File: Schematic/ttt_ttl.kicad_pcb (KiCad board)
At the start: 2 copper layers, 79.8 x 129.5 mm, 79 parts, among them J1 Conn_01x01, J2 Conn_01x01, SW1 SW_Push, SW10 SW_Push, SW2 SW_Push, SW3 SW_Push, SW4 SW_Push, SW5 SW_Push, SW6 SW_Push, SW7 SW_Push, SW8 SW_Push, SW9 SW_Push, U1 74LS109, U10 27C2001, U11 74LS154, U12 NE555, U2 74LS109, U3 74LS109, U4 74LS109, U5 74LS109, U6 74LS109, U7 74LS109, U8 74LS109, U9 74LS109

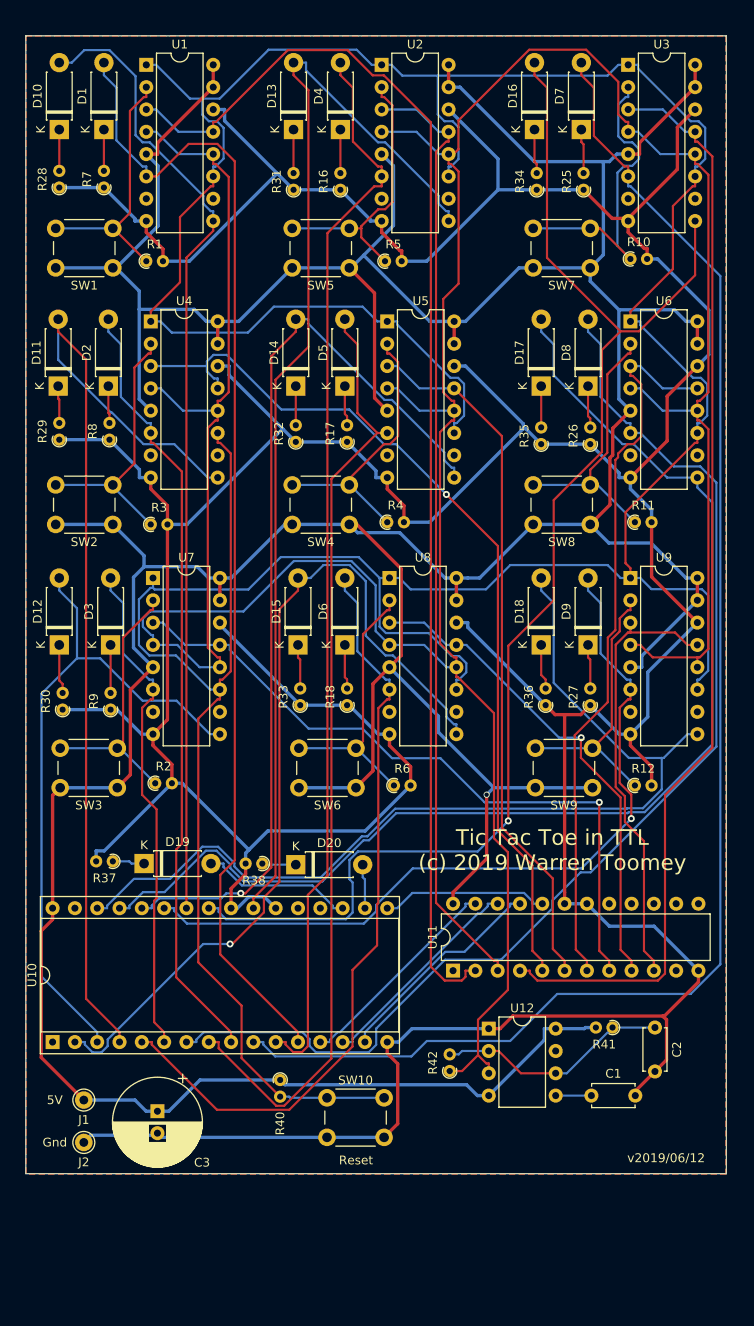
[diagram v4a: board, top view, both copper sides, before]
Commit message: Smaller 8Kx8 EEPROM is working
I managed to get the code to generate a ROM file which uses a 4-bit board
state plus the user's moves to look up the net board move and the next
board state. I've redone the schematic, PCB and I've started on the
documentation. I need to redraw the design diagram.
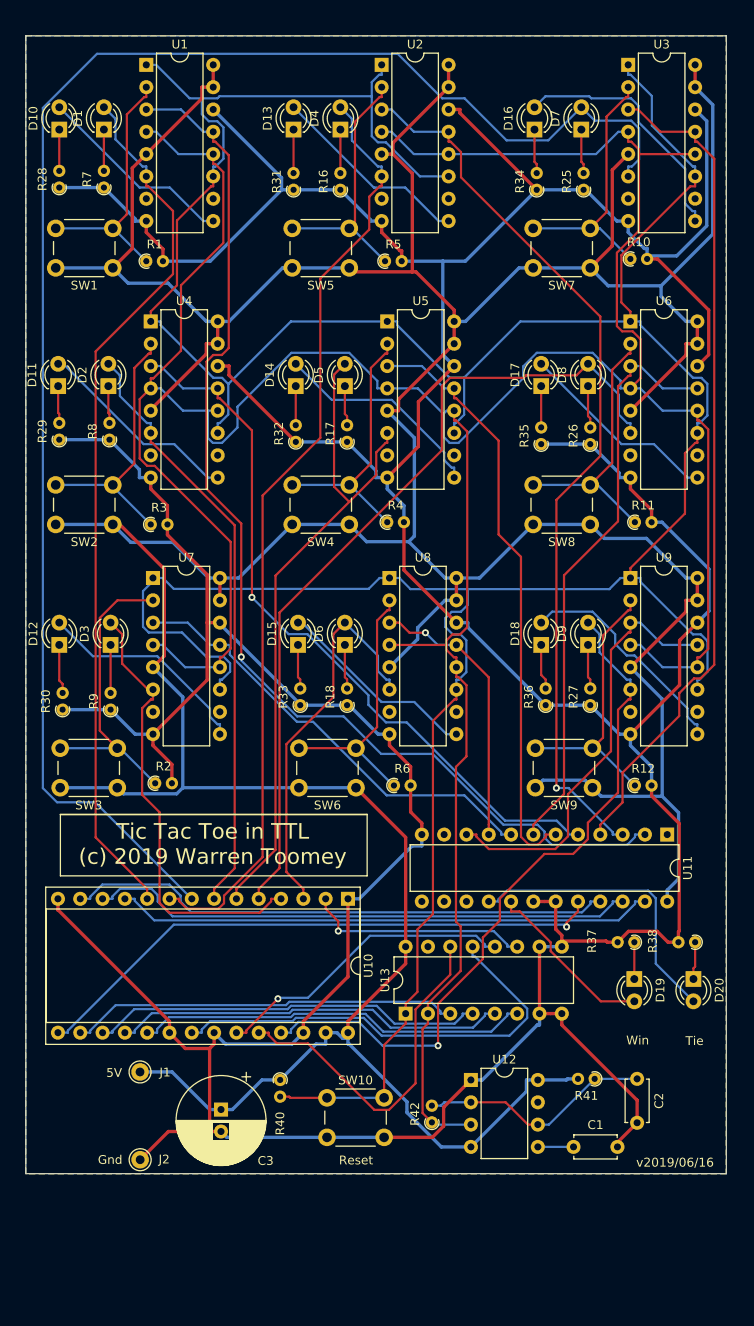
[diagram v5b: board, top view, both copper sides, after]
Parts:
- added U13: 74LS161, Package_DIP:DIP-16_W7.62mm, F.Cu at (67.4, 134.9)
- D1, D10, D11, D12, D13, D14, D15, D16, D17, D18, D19, D2, D20, D3, D4, D5, D6, D7, D8, D9: footprint Diode_THT:D_DO-41_SOD81_P7.62mm_Horizontal -> LED_THT:LED_D3.0mm
- U10: value 27C2001 -> 28C256; footprint Package_DIP:DIP-32_W15.24mm_Socket -> Package_DIP:DIP-28_W15.24mm_Socket
- moved R37 60.1 mm to (93.4, 126.8)
- moved D19 57.3 mm to (93.4, 131.0), turned to 270 degrees
- moved R38 50.1 mm to (100.3, 126.8)
- moved D20 47.1 mm to (100.1, 131.0), turned to 270 degrees
- moved U10 37.4 mm to (60.8, 121.9), turned to 270 degrees
- moved U11 28.9 mm to (97.2, 114.6), turned to 270 degrees
- moved C3 7.24 mm to (46.4, 145.9)
- moved J1 7.16 mm to (37.1, 141.6)
- moved J2 6.71 mm to (37.1, 151.6)
- moved C1 6.19 mm to (86.5, 150.1)
- moved U12 6.19 mm to (74.8, 142.5)
- moved R41 6.19 mm to (88.9, 142.4)
- moved C2 6.19 mm to (93.7, 142.4)
- moved R42 6.19 mm to (70.4, 147.3)
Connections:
- D10 pad 2: Board1 -> Net-(D10-Pad2)
- D11 pad 2: Board4 -> Net-(D11-Pad2)
- D12 pad 2: Board7 -> Net-(D12-Pad2)
- D13 pad 2: Board2 -> Net-(D13-Pad2)
- D14 pad 2: Board5 -> Net-(D14-Pad2)
- D15 pad 2: Board8 -> Net-(D15-Pad2)
- D16 pad 2: Board3 -> Net-(D16-Pad2)
- D17 pad 2: Board6 -> Net-(D17-Pad2)
- D18 pad 2: Board9 -> Net-(D18-Pad2)
- U1 pad 9: Board1 -> Net-(D10-Pad2)
- U10 pad 1: Net-(U10-Pad1) -> Lo
- U10 pad 10: User3 -> User1
- U10 pad 11: User2 -> Net-(U10-Pad11)
- U10 pad 12: User1 -> Net-(U10-Pad12)
- U10 pad 14: Net-(U10-Pad14) -> Lo
- U10 pad 16: Lo -> Net-(U10-Pad16)
- U10 pad 18: Net-(D20-Pad2) -> Net-(U10-Pad18)
- U10 pad 19: Net-(D19-Pad2) -> Net-(U10-Pad19)
- U10 pad 2: Board8 -> Newstate3
- U10 pad 20: Net-(U10-Pad20) -> Lo
- U10 pad 21: Net-(U10-Pad21) -> Newstate1
- U10 pad 23: Board2 -> Newstate2
- U10 pad 24: Lo -> Newstate0
- U10 pad 25: Board3 -> User9
- U10 pad 26: Board1 -> Lo
- U10 pad 27: User9 -> Hi
- U10 pad 28: Board5 -> Hi
- U10 pad 3: Board7 -> User8
- U10 pad 4: Board4 -> User7
- U10 pad 5: User8 -> User6
- U10 pad 6: User7 -> User5
- U10 pad 7: User6 -> User4
- U10 pad 8: User5 -> User3
- U10 pad 9: User4 -> User2
- U11 pad 16: Net-(U11-Pad16) -> Net-(D20-Pad2)
- U11 pad 17: Net-(U11-Pad17) -> Net-(D19-Pad2)
- U11 pad 20: Net-(U10-Pad17) -> Net-(U10-Pad15)
- U11 pad 21: Net-(U10-Pad15) -> Net-(U10-Pad13)
- U11 pad 22: Net-(U10-Pad14) -> Net-(U10-Pad12)
- U11 pad 23: Net-(U10-Pad13) -> Net-(U10-Pad11)
- U2 pad 9: Board2 -> Net-(D13-Pad2)
- U3 pad 9: Board3 -> Net-(D16-Pad2)
- U4 pad 9: Board4 -> Net-(D11-Pad2)
- U5 pad 9: Board5 -> Net-(D14-Pad2)
- U6 pad 9: Board6 -> Net-(D17-Pad2)
- U7 pad 9: Board7 -> Net-(D12-Pad2)
- U8 pad 9: Board8 -> Net-(D15-Pad2)
- U9 pad 9: Board9 -> Net-(D18-Pad2)
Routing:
- net Board3: track 156.5 -> 0.00 mm, vias 1 -> 0
- net Board6: track 137.8 -> 0.00 mm
- net Board2: track 126.4 -> 0.00 mm
- net Board4: track 113.5 -> 0.00 mm
- net Board1: track 110.8 -> 0.00 mm
- net Board9: track 110.3 -> 0.00 mm
- net Board5: track 107.4 -> 0.00 mm, vias 1 -> 0
- net Board8: track 100.3 -> 0.00 mm, vias 1 -> 0
- net Board7: track 77.8 -> 0.00 mm
- net Net-(U10-Pad12): track 0.00 -> 62.4 mm
- net Net-(U10-Pad11): track 0.00 -> 61.4 mm
- net Newstate1: track 0.00 -> 51.6 mm
- net Net-(U10-Pad19): track 0.00 -> 45.1 mm
- net Net-(U10-Pad18): track 0.00 -> 45.0 mm
- net Net-(U10-Pad16): track 0.00 -> 44.4 mm
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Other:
- board text added: "Tie"
- board text added: "Win"
- board text added: "v2019/06/16"
- board text removed: "v2019/06/12"

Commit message: I bought different pushbuttons, so I updated the PCB design.
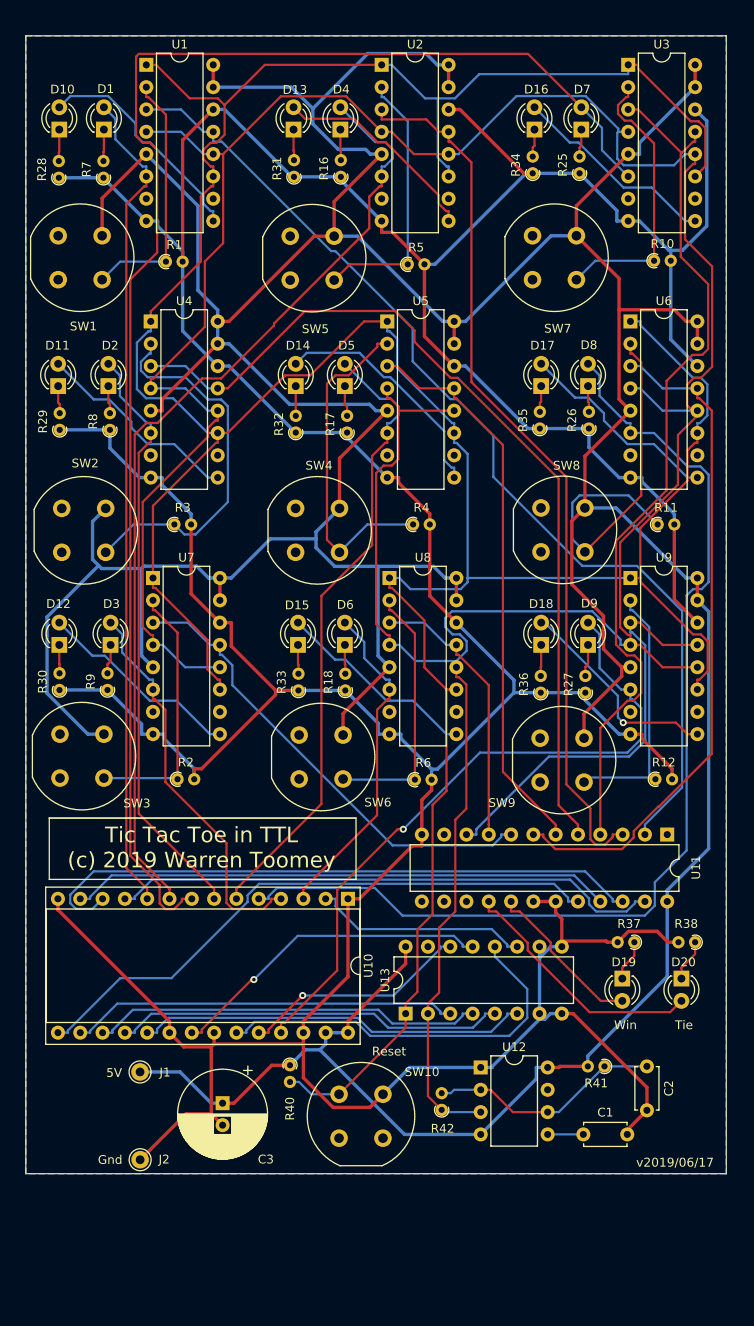
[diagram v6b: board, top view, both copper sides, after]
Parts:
- SW1, SW10, SW2, SW3, SW4, SW5, SW6, SW7, SW8, SW9: footprint Button_Switch_THT:SW_PUSH_6mm_H8mm -> Button_Switch_THT:Push_E-Switch_KS01Q01
- moved SW3 6.28 mm to (33.0, 103.1), turned to 270 degrees
- moved SW6 6.17 mm to (60.2, 103.2), turned to 270 degrees
- moved SW9 5.72 mm to (87.7, 103.6), turned to 270 degrees
- moved SW5 4.00 mm to (59.2, 46.4), turned to 270 degrees
- moved SW7 3.98 mm to (86.8, 46.4), turned to 270 degrees
- moved SW1 3.86 mm to (32.8, 46.4), turned to 270 degrees
- moved R4 2.96 mm to (68.2, 79.2)
- moved R10 2.70 mm to (95.7, 49.2)
- moved R3 2.69 mm to (41.0, 79.2)
- moved R5 2.62 mm to (67.6, 49.6)
- moved R11 2.60 mm to (96.1, 79.2)
- moved R2 2.58 mm to (41.4, 108.3)
- moved R6 2.48 mm to (68.4, 108.3)
- moved R12 2.44 mm to (95.8, 108.3)
- moved R30 2.26 mm to (28.0, 98.1)
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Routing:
- net User6: track 94.8 -> 120.7 mm
- net Move4: track 83.3 -> 101.2 mm, vias 1 -> 0
- net User3: track 182.9 -> 168.6 mm
- net Newstate1: track 51.6 -> 37.4 mm, vias 0 -> 1
- net Newstate0: track 40.1 -> 26.2 mm, vias 0 -> 1
- net Net-(R11-Pad1): track 31.4 -> 44.6 mm
- net Reset: track 404.9 -> 391.8 mm
- net Net-(R3-Pad1): track 30.8 -> 43.3 mm
- net Move1: track 128.7 -> 117.5 mm, vias 1 -> 0
- net Move6: track 66.7 -> 77.2 mm
- net Newstate2: track 34.8 -> 44.9 mm, vias 1 -> 0
- net Net-(U10-Pad12): track 62.4 -> 71.0 mm
- net Lo: track 619.6 -> 611.4 mm
- net Net-(R4-Pad1): track 30.6 -> 38.4 mm
- net Clk: track 382.8 -> 375.6 mm
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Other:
- board text added: "v2019/06/17"
- board text removed: "v2019/06/16"

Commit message: Small circuit change. Tie/win LEDs must connect to demux active low output.
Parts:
- moved R38 11.9 mm to (91.2, 134.4), turned to 0 degrees
- moved R37 8.86 mm to (98.0, 134.4), turned to 0 degrees
- moved D19 7.01 mm to (99.0, 130.1), turned to 90 degrees
- moved D20 6.31 mm to (92.5, 130.0), turned to 90 degrees
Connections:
- D19 pad 2: Net-(D19-Pad2) -> Hi
- D20 pad 2: Net-(D20-Pad2) -> Hi
- R37 pad 1: Net-(D19-Pad1) -> Net-(R37-Pad1)
- R37 pad 2: Lo -> Net-(D19-Pad1)
- R38 pad 1: Net-(D20-Pad1) -> Net-(R38-Pad1)
- R38 pad 2: Lo -> Net-(D20-Pad1)
- U11 pad 16: Net-(D20-Pad2) -> Net-(R38-Pad1)
- U11 pad 17: Net-(D19-Pad2) -> Net-(R37-Pad1)
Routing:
- net Net-(D20-Pad2): track 28.8 -> 0.00 mm
- net Net-(R37-Pad1): track 0.00 -> 27.3 mm
- net Net-(R38-Pad1): track 0.00 -> 20.6 mm
- net Net-(D19-Pad2): track 18.6 -> 0.00 mm
- net Lo: track 611.4 -> 596.0 mm
- net Clk: track 375.6 -> 364.5 mm
- net User3: track 168.6 -> 157.7 mm
- net Move4: track 101.2 -> 90.6 mm, vias 0 -> 1
- net Net-(U10-Pad12): track 71.0 -> 62.5 mm
- net Net-(R3-Pad1): track 43.3 -> 35.1 mm
- net Net-(D16-Pad2): track 23.7 -> 31.6 mm
- net Net-(R11-Pad1): track 44.6 -> 36.7 mm
- net User6: track 120.7 -> 114.0 mm
- net Hi: track 583.4 -> 589.8 mm
- net Net-(R1-Pad1): track 29.0 -> 34.8 mm
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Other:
- board text added: "v2019/06/18"
- board text removed: "v2019/06/17"

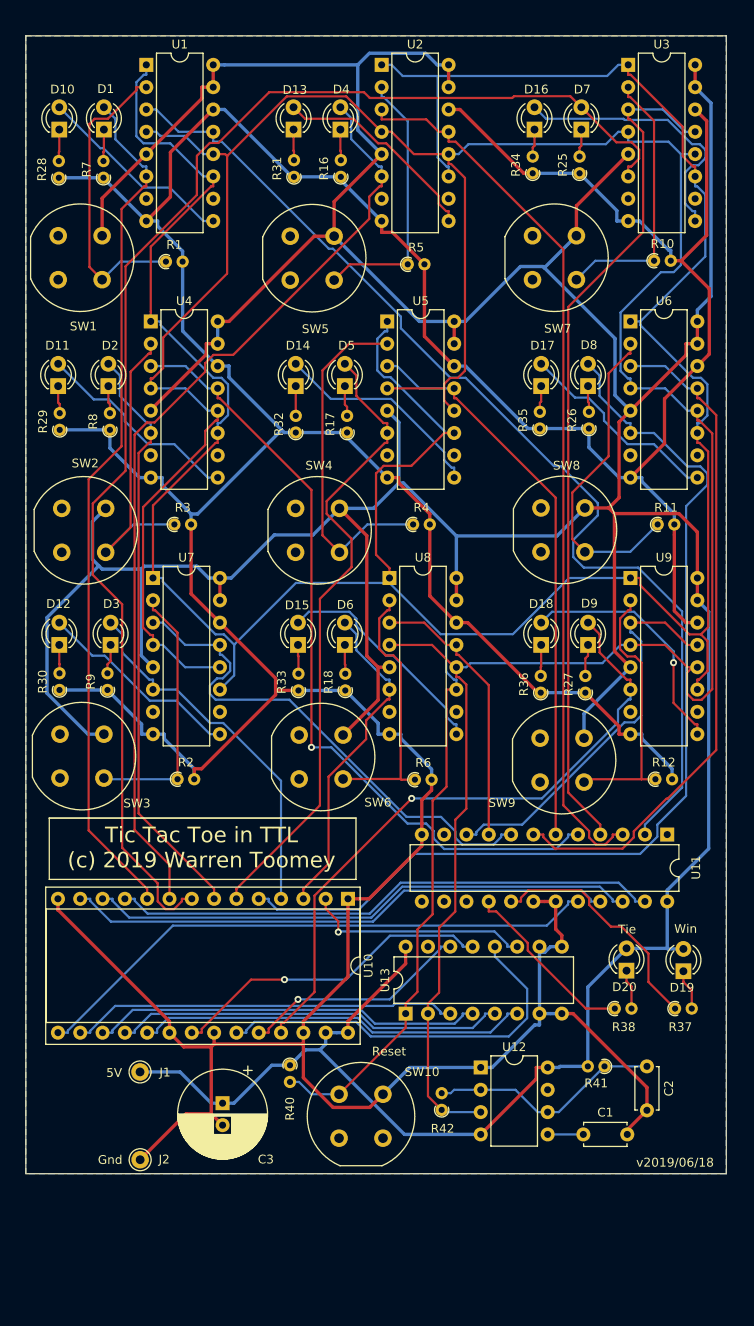
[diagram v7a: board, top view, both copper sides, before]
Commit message: Changed to horizontal resistors on PCB.
This resulted in only two vias, so that's nice.
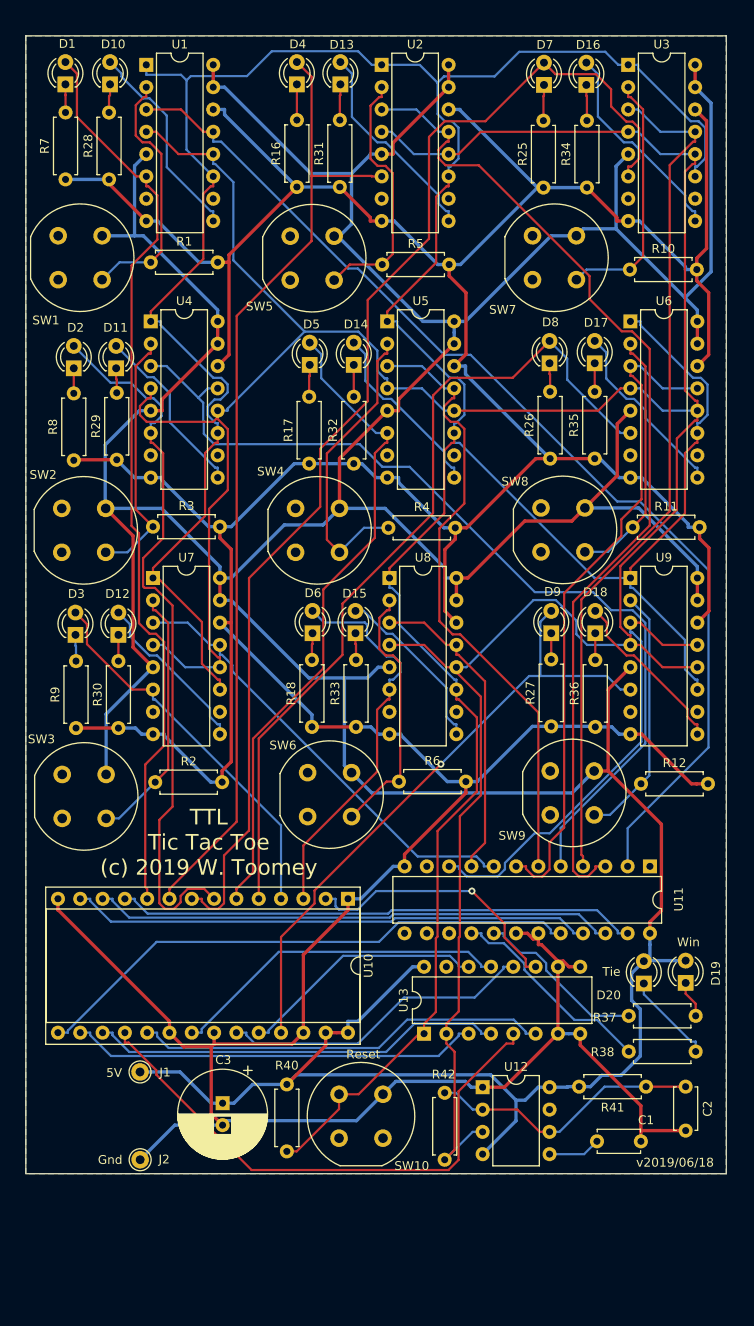
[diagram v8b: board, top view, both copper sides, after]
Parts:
- R1, R10, R11, R12, R16, R17, R18, R2, R25, R26, R27, R28, R29, R3, R30, R31, R32, R33, R34, R35, R36, R37, R38, R4, R40, R41, R42, R5, R6, R7, R8, R9: footprint Resistor_THT:R_Axial_DIN0204_L3.6mm_D1.6mm_P1.90mm_Vertical -> Resistor_THT:R_Axial_DIN0207_L6.3mm_D2.5mm_P7.62mm_Horizontal
- moved R30 7.98 mm to (34.7, 102.4)
- moved D16 7.79 mm to (87.9, 29.2)
- moved R33 7.76 mm to (61.7, 102.3)
- moved D10 7.74 mm to (33.7, 29.1)
- moved R32 7.49 mm to (61.5, 72.3)
- moved D13 7.41 mm to (59.9, 29.1)
- moved R36 7.33 mm to (89.0, 102.3)
- moved R29 7.33 mm to (34.5, 71.9)
- moved D4 7.14 mm to (55.0, 29.1)
- moved R35 7.13 mm to (88.9, 71.8)
- moved D14 7.03 mm to (61.5, 61.1)
- moved D11 6.91 mm to (34.4, 61.5)
- moved D12 6.83 mm to (34.7, 91.8)
- moved D1 6.76 mm to (28.6, 29.1)
- moved D15 6.68 mm to (61.7, 91.6)
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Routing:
- net Net-(U10-Pad18): track 44.7 -> 63.3 mm
- net User3: track 157.7 -> 139.4 mm
- net User6: track 114.0 -> 96.3 mm
- net User4: track 67.4 -> 82.9 mm
- net Move4: track 90.6 -> 104.8 mm, vias 1 -> 0
- net Move2: track 101.6 -> 114.4 mm
- net Newstate2: track 45.0 -> 36.0 mm
- net Net-(D18-Pad2): track 28.2 -> 19.5 mm, vias 1 -> 0
- net Hi: track 589.8 -> 582.0 mm
- net Net-(R11-Pad1): track 36.7 -> 29.0 mm
- net Net-(D16-Pad2): track 31.6 -> 23.9 mm
- net Lo: track 596.0 -> 603.5 mm
- net Net-(R37-Pad1): track 27.3 -> 19.9 mm
- net Move7: track 58.7 -> 51.5 mm
- net User8: track 38.0 -> 45.1 mm
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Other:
- board text added: "TTL Tic Tac Toe (c) 2019 W. Toomey"
- board text removed: "Tic Tac Toe in TTL (c) 2019 Warren Toomey"
